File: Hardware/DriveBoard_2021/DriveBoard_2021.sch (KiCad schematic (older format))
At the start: 80 parts, among them SW1 SW_Push, SW2 SW_Push, SW3 SW_Push, SW4 SW_Push, SW5 SW_Push, SW6 SW_Push, U1 TM4C129E_Launchpad, U2 LM2576S-3.3, U3 LM2576HVS-5, U4 MCP2551-I-SN

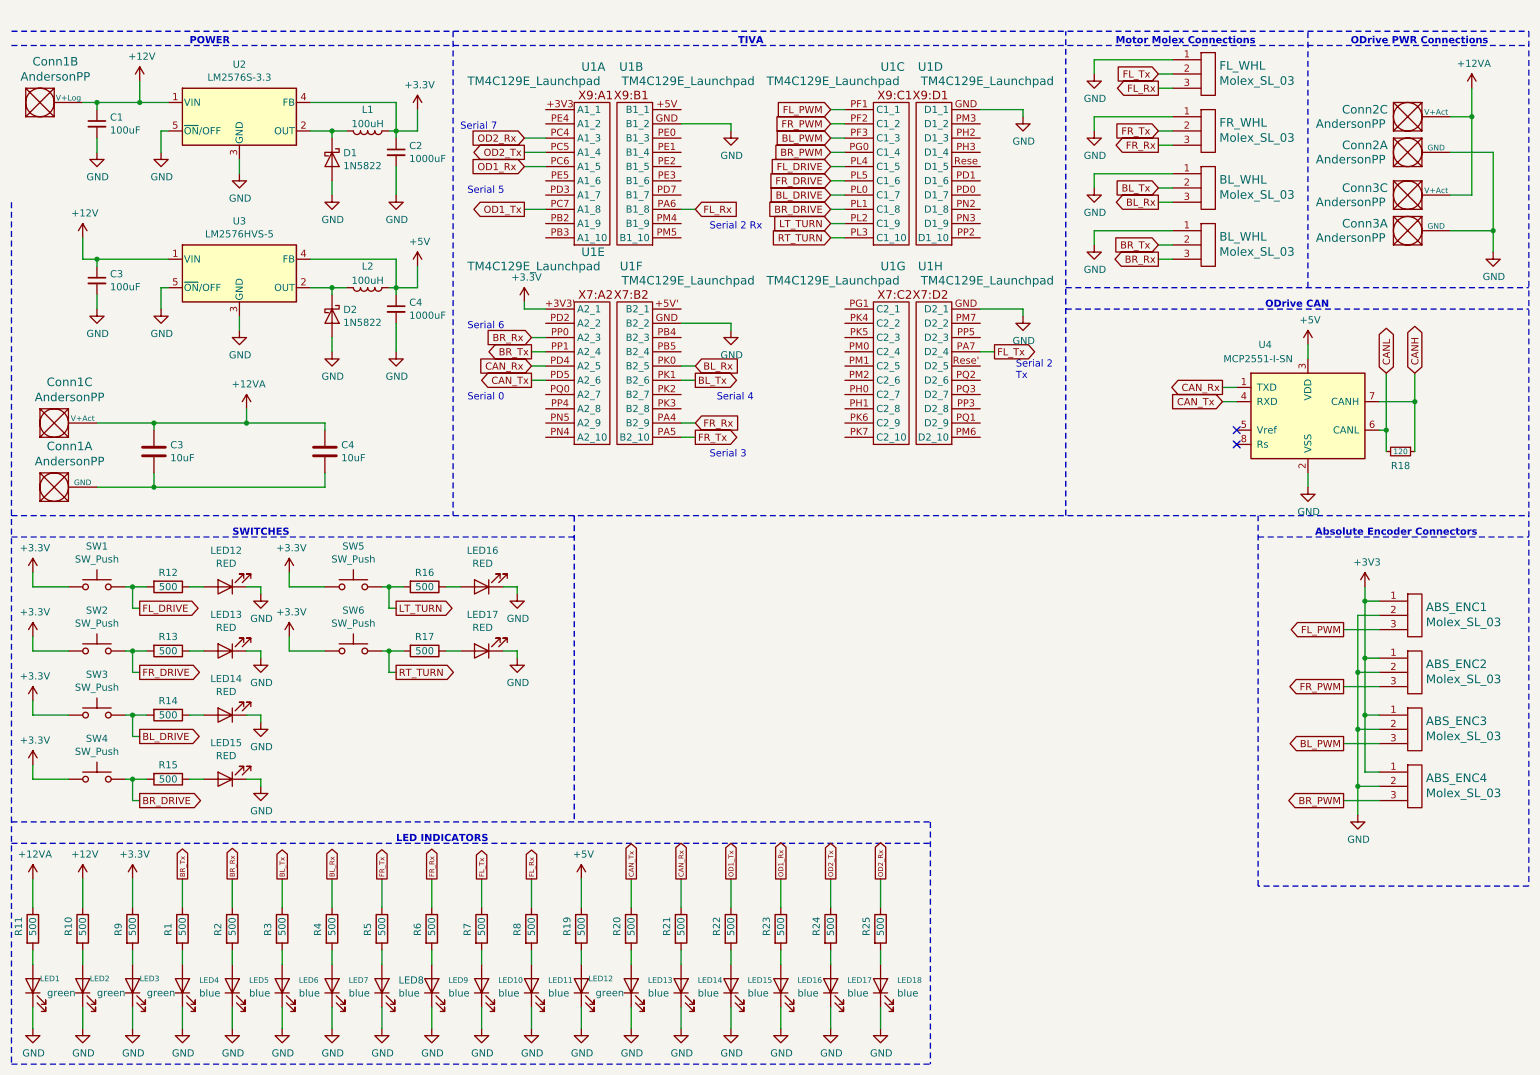
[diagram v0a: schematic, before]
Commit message: Added ODrive Data Connectors, Switched schematic page size, removed 12 Logic bus
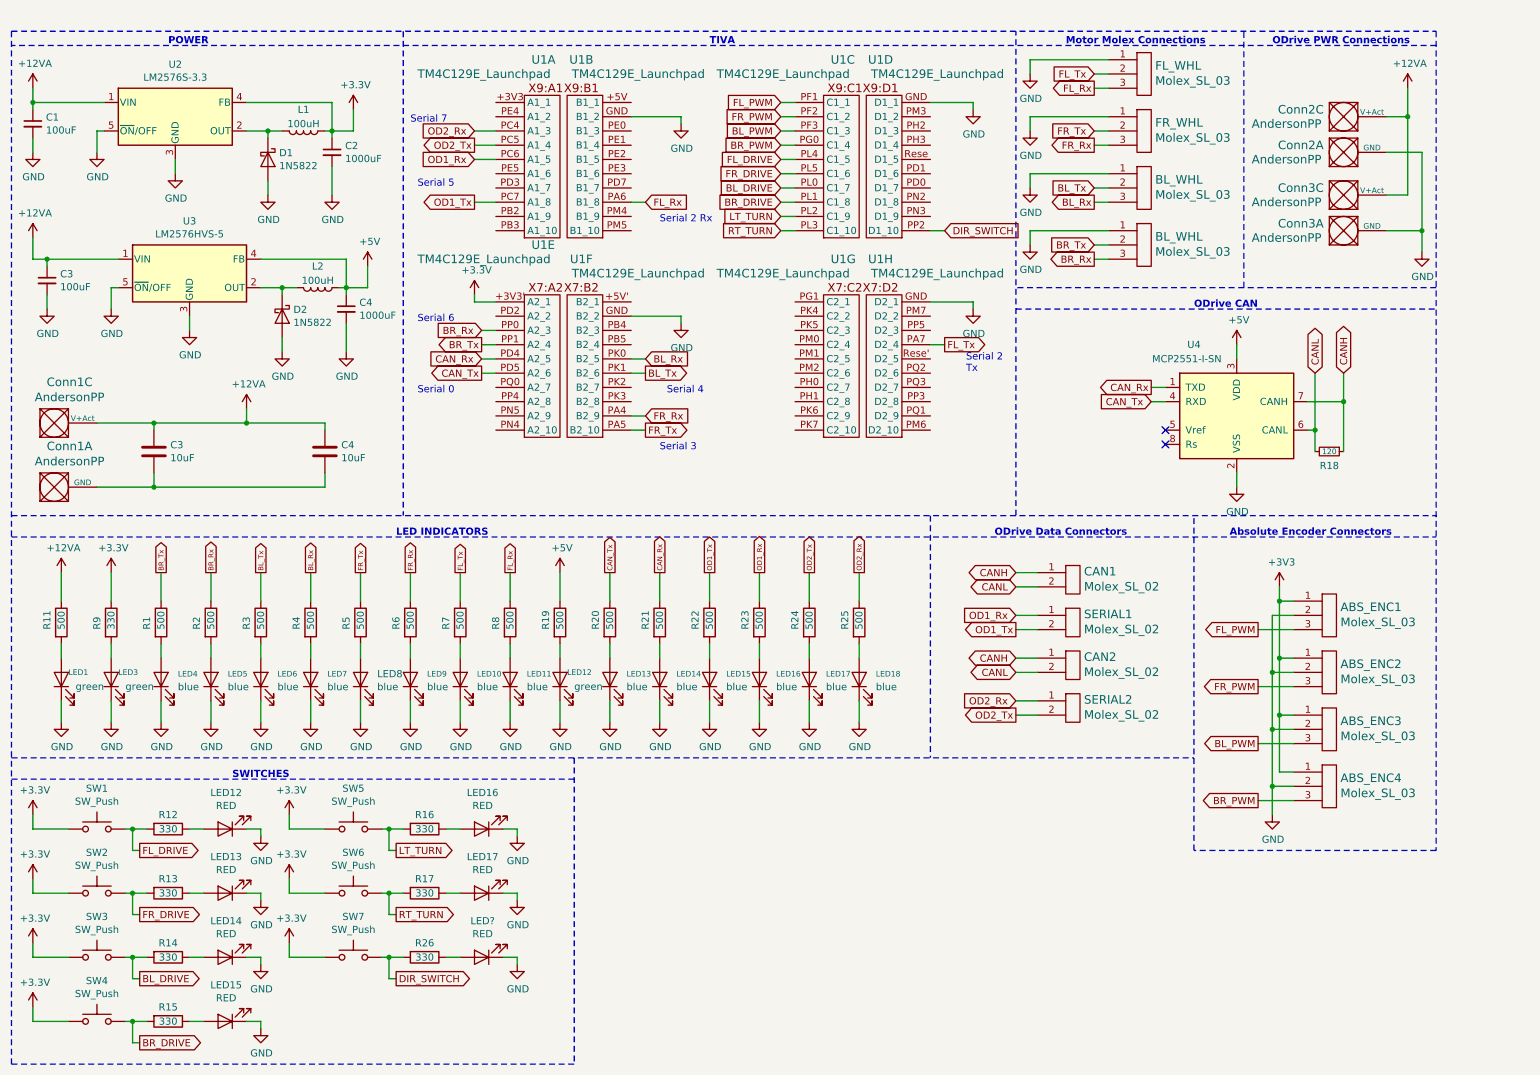
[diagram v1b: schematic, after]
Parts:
- removed unit 2 of Conn1
- removed LED2: green, symbol Device:LED
- removed R10: 500, symbol Device:R
- added CAN1, CAN2, SERIAL1, SERIAL2: Molex_SL_02, symbol MRDT_Connectors:Molex_SL_02
- added LED?: RED, symbol Device:LED
- added R26: 330, symbol Device:R
- added SW7: SW_Push, symbol Switch:SW_Push
- R12, R13, R14, R15, R16, R17, R9: value 500 -> 330
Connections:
- net +12V is gone; now on net +12VA: C1.1, C3.1, U2.1 (VIN), U3.1 (VIN)
- net +3V3: now also SW7.1
- net CANH: now also CAN1.1, CAN2.1
- net CANL: now also CAN1.2, CAN2.2
- net GND: now also LED?.1 (K)
- net OD1_Rx: now also SERIAL1.1
- net OD1_Tx: now also SERIAL1.2
- net OD2_Rx: now also SERIAL2.1
- net OD2_Tx: now also SERIAL2.2
- net DIR_SWITCH: now reaches U1.PP2 (D1_10)
- net DIR_SWITCH: now also R26.2, SW7.2
- new net: LED?.2 (A), R26.1
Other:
- note added: "ODrive Data Connectors"
- moved on the sheet: ABS_ENC1, ABS_ENC2, ABS_ENC3, ABS_ENC4, BL_WHL, C1, C2, C3, C4, Conn2A, Conn2C, Conn3A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

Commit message: Updated LEDs, Organized file layout, removed old files
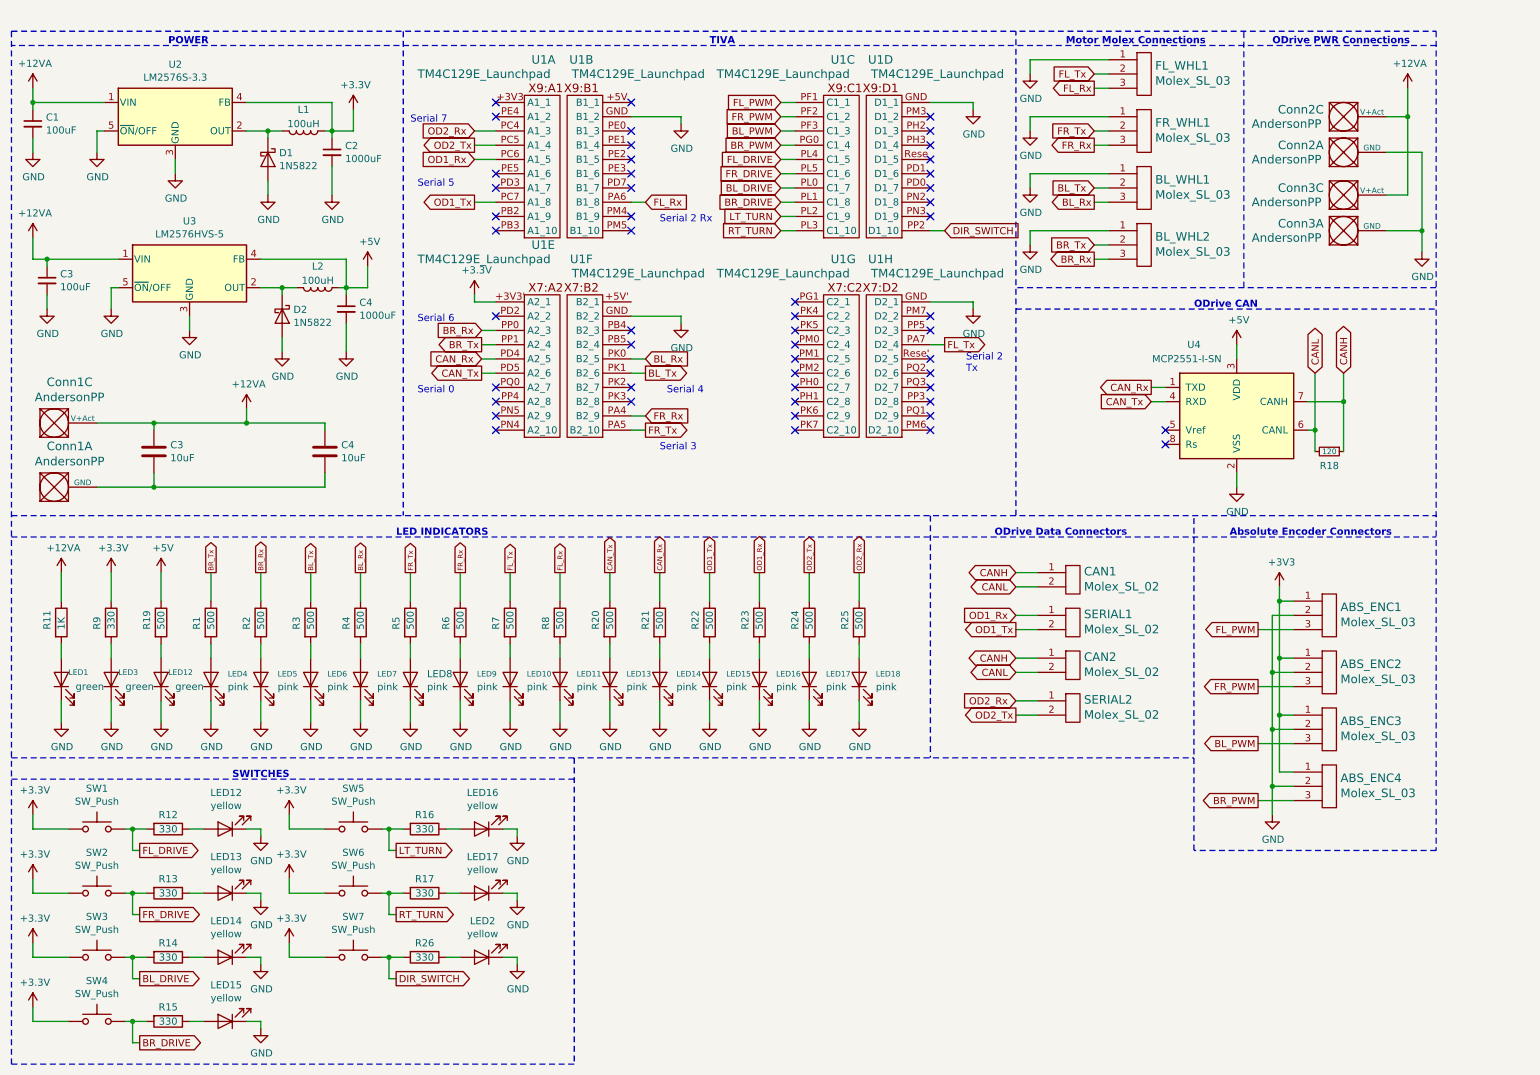
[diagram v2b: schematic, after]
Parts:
- LED10, LED11, LED13, LED14, LED15, LED16, LED17, LED18, LED4, LED5, LED6, LED7, LED8, LED9: value blue -> pink
- LED12, LED13, LED14, LED15, LED16, LED17: value RED -> yellow
- LED2: renamed from LED?; value RED -> yellow
- R11: value 500 -> 1K
- renumbered BL_WHL to BL_WHL1, BL_WHL to BL_WHL2, FL_WHL to FL_WHL1, FR_WHL to FR_WHL1
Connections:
- no-connect marks 2 -> 51
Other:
- moved on the sheet: LED10, LED11, LED12, LED4, LED5, LED6, LED7, LED8, LED9, R1, R19, R2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

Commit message: Fixed ODrive Serial Lines, Added Ferrite Beads to ODrive PWR
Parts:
- removed SERIAL1, SERIAL2: Molex_SL_02, symbol MRDT_Connectors:Molex_SL_02
- added FB1, FB2: Ferrite_Bead_Small, symbol Device:Ferrite_Bead_Small
- added SERIAL1, SERIAL2: Molex_SL_03, symbol MRDT_Connectors:Molex_SL_03
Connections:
- wire segments 258 -> 263
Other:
- moved on the sheet: CAN2
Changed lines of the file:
@@
-$Comp
-L MRDT_Connectors:AndersonPP Conn1
-U 3 1 5F623BE1
-P 700 3350
-F 0 "Conn1" H 908 3737 60  0000 C CNN
-F 1 "AndersonPP" H 908 3631 60  0000 C CNN
-F 2 "" H 550 2800 60  0001 C CNN
-F 3 "" H 550 2800 60  0001 C CNN
-	3    700  3350
-	1    0    0    -1
-$EndComp
 $Comp
 L MRDT_Connectors:AndersonPP Conn1
@@
 Wire Wire Line
 	2700 3600 2700 3700
-Wire Wire Line
-	1100 3250 1500 3250
-Connection ~ 1500 3250
 Wire Wire Line
 	1500 3250 2150 3250
@@
 L power:+12VA #PWR0144
 U 1 1 5F84828D
-P 10300 900
-F 0 "#PWR0144" H 10300 750 50  0001 C CNN
-F 1 "+12VA" H 10315 1073 50  0000 C CNN
-F 2 "" H 10300 900 50  0001 C CNN
-F 3 "" H 10300 900 50  0001 C CNN
-	1    10300 900
+P 10300 800
+F 0 "#PWR0144" H 10300 650 50  0001 C CNN
+F 1 "+12VA" H 10315 973 50  0000 C CNN
+F 2 "" H 10300 800 50  0001 C CNN
+F 3 "" H 10300 800 50  0001 C CNN
+	1    10300 800
 	1    0    0    -1
 $EndComp
@@
 $EndComp
 Wire Wire Line
-	10300 900  10300 1100
-Wire Wire Line
 	10300 1100 10150 1100
 Wire Wire Line
-	10300 1100 10300 1650
-Wire Wire Line
 	10300 1650 10150 1650
-Connection ~ 10300 1100
 Text Notes 9350 600  0    50   ~ 10
 ODrive PWR Connections
@@
 $EndComp
 Wire Notes Line
-	6950 3900 6950 5600
-Wire Notes Line
 	4450 5600 4450 7750
 Text Notes 8800 2450 0    50   ~ 10
@@
 $EndComp
 $Comp
-L MRDT_Connectors:Molex_SL_02 SERIAL1
-U 1 1 5F8803F7
-P 7900 4750
-F 0 "SERIAL1" H 8028 4908 60  0000 L CNN
-F 1 "Molex_SL_02" H 8028 4802 60  0000 L CNN
-F 2 "" H 7900 4650 60  0001 C CNN
-F 3 "" H 7900 4650 60  0001 C CNN
-	1    7900 4750
-	1    0    0    -1
-$EndComp
-$Comp
 L MRDT_Connectors:Molex_SL_02 CAN2
 U 1 1 5F8813EB
-P 7900 5050
-F 0 "CAN2" H 8028 5208 60  0000 L CNN
-F 1 "Molex_SL_02" H 8028 5102 60  0000 L CNN
-F 2 "" H 7900 4950 60  0001 C CNN
-F 3 "" H 7900 4950 60  0001 C CNN
-	1    7900 5050
-	1    0    0    -1
-$EndComp
-$Comp
-L MRDT_Connectors:Molex_SL_02 SERIAL2
-U 1 1 5F8813F1
 P 7900 5350
-F 0 "SERIAL2" H 8028 5508 60  0000 L CNN
+F 0 "CAN2" H 8028 5508 60  0000 L CNN
 F 1 "Molex_SL_02" H 8028 5402 60  0000 L CNN
 F 2 "" H 7900 5250 60  0001 C CNN
@@
 Text GLabel 7550 4400 0    50   BiDi ~ 0
 CANL
-Text GLabel 7550 4900 0    50   BiDi ~ 0
+Text GLabel 7550 5200 0    50   BiDi ~ 0
 CANH
-Text GLabel 7550 5000 0    50   BiDi ~ 0
+Text GLabel 7550 5300 0    50   BiDi ~ 0
 CANL
 Wire Wire Line
@@
 	7550 4400 7700 4400
 Wire Wire Line
-	7550 4900 7700 4900
-Wire Wire Line
-	7550 5000 7700 5000
+	7550 5200 7700 5200
+Wire Wire Line
+	7550 5300 7700 5300
 Text GLabel 7550 4600 0    50   Input ~ 0
 OD1_Rx
-Text GLabel 7550 4700 0    50   Output ~ 0
+Text GLabel 7550 4800 0    50   Output ~ 0
 OD1_Tx
 Wire Wire Line
-	7550 4700 7700 4700
-Wire Wire Line
 	7550 4600 7700 4600
-Text GLabel 7550 5200 0    50   Input ~ 0
-OD2_Rx
-Text GLabel 7550 5300 0    50   Output ~ 0
-OD2_Tx
-Wire Wire Line
-	7550 5200 7700 5200
-Wire Wire Line
-	7550 5300 7700 5300
 Wire Wire Line
 	10150 1350 10400 1350
@@
 	7550 2450 10500 2450
 Wire Notes Line
-	10500 6250 8800 6250
-Wire Notes Line
 	8800 6250 8800 3900
 Wire Notes Line
@@
 Wire Notes Line
 	500  4050 10500 4050
-Wire Notes Line
-	500  5600 8800 5600
 Text Notes 7400 4050 0    50   ~ 10
 ODrive Data Connectors
@@
 NoConn ~ 3900 3000
 NoConn ~ 3900 2500
+Wire Notes Line
+	6950 5600 500  5600
+$Comp
+L MRDT_Connectors:Molex_SL_03 SERIAL1
+U 1 1 5F8B8A8B
+P 7900 4850
+F 0 "SERIAL1" H 8028 5058 60  0000 L CNN
+F 1 "Molex_SL_03" H 8028 4952 60  0000 L CNN
+F 2 "" H 7900 4850 60  0001 C CNN
+F 3 "" H 7900 4850 60  0001 C CNN
+	1    7900 4850
+	1    0    0    -1
+$EndComp
+Wire Wire Line
+	7700 4800 7550 4800
+$Comp
+L power:GND #PWR?
+U 1 1 5F8DC5C8
+P 7650 4900
+F 0 "#PWR?" H 7650 4650 50  0001 C CNN
+F 1 "GND" H 7655 4727 50  0000 C CNN
+F 2 "" H 7650 4900 50  0001 C CNN
+F 3 "" H 7650 4900 50  0001 C CNN
+	1    7650 4900
+	1    0    0    -1
+$EndComp
+Wire Wire Line
+	7650 4900 7650 4700
+Wire Wire Line
+	7650 4700 7700 4700
+Wire Wire Line
+	7550 5550 7700 5550
+Wire Wire Line
+	7700 5750 7550 5750
+$Comp
+L power:GND #PWR?
+U 1 1 5F8FFE40
+P 7650 5850
+F 0 "#PWR?" H 7650 5600 50  0001 C CNN
+F 1 "GND" H 7655 5677 50  0000 C CNN
+F 2 "" H 7650 5850 50  0001 C CNN
+F 3 "" H 7650 5850 50  0001 C CNN
+	1    7650 5850
+	1    0    0    -1
+$EndComp
+Wire Wire Line
+	7650 5850 7650 5650
+Wire Wire Line
+	7650 5650 7700 5650
+Connection ~ 1500 3250
+Wire Wire Line
+	1100 3250 1500 3250
+$Comp
+L MRDT_Connectors:AndersonPP Conn1
+U 3 1 5F623BE1
+P 700 3350
+F 0 "Conn1" H 908 3737 60  0000 C CNN
+F 1 "AndersonPP" H 908 3631 60  0000 C CNN
+F 2 "" H 550 2800 60  0001 C CNN
+F 3 "" H 550 2800 60  0001 C CNN
+	3    700  3350
+	1    0    0    -1
+$EndComp
+Text GLabel 7550 5550 0    50   Input ~ 0
+OD2_Rx
+Text GLabel 7550 5750 0    50   Output ~ 0
+OD2_Tx
+$Comp
+L MRDT_Connectors:Molex_SL_03 SERIAL2
+U 1 1 5F8FFE39
+P 7900 5800
+F 0 "SERIAL2" H 8028 6008 60  0000 L CNN
+F 1 "Molex_SL_03" H 8028 5902 60  0000 L CNN
+F 2 "" H 7900 5800 60  0001 C CNN
+F 3 "" H 7900 5800 60  0001 C CNN
+	1    7900 5800
+	1    0    0    -1
+$EndComp
+Wire Notes Line
+	6950 6250 10500 6250
+Wire Notes Line
+	6950 3900 6950 6250
+$Comp
+L Device:Ferrite_Bead_Small FB1
+U 1 1 5F9B9929
+P 10300 950
+F 0 "FB1" H 10100 1000 50  0000 L CNN
+F 1 "Ferrite_Bead_Small" H 9450 1000 50  0001 L CNN
+F 2 "" V 10230 950 50  0001 C CNN
+F 3 "~" H 10300 950 50  0001 C CNN
+	1    10300 950
+	1    0    0    -1
+$EndComp
+Wire Wire Line
+	10300 1050 10300 1100
+Wire Wire Line
+	10300 850  10300 800
+$Comp
+L Device:Ferrite_Bead_Small FB2
+U 1 1 5FA2512E
+P 10300 1550
+F 0 "FB2" H 10100 1650 50  0000 L CNN
+F 1 "Ferrite_Bead_Small" H 10400 1505 50  0001 L CNN
+F 2 "" V 10230 1550 50  0001 C CNN
+F 3 "~" H 10300 1550 50  0001 C CNN
+	1    10300 1550
+	1    0    0    -1
+$EndComp
+Wire Wire Line
+	10300 1450 10300 1100
+Connection ~ 10300 1100
 $EndSCHEMATC
